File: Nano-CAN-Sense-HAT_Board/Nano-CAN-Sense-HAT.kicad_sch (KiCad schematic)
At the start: 44 parts, among them J1 Analog, J2 Digital, J3 Conn_02x04_Counter_Clockwise, J4 Conn_02x04_Counter_Clockwise, J5 Conn_01x05, J6 Conn_01x03, SW1 SW_Push, SW2 SW_Push, U1 LMC6484, U2 MCP2518FD-xQBB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

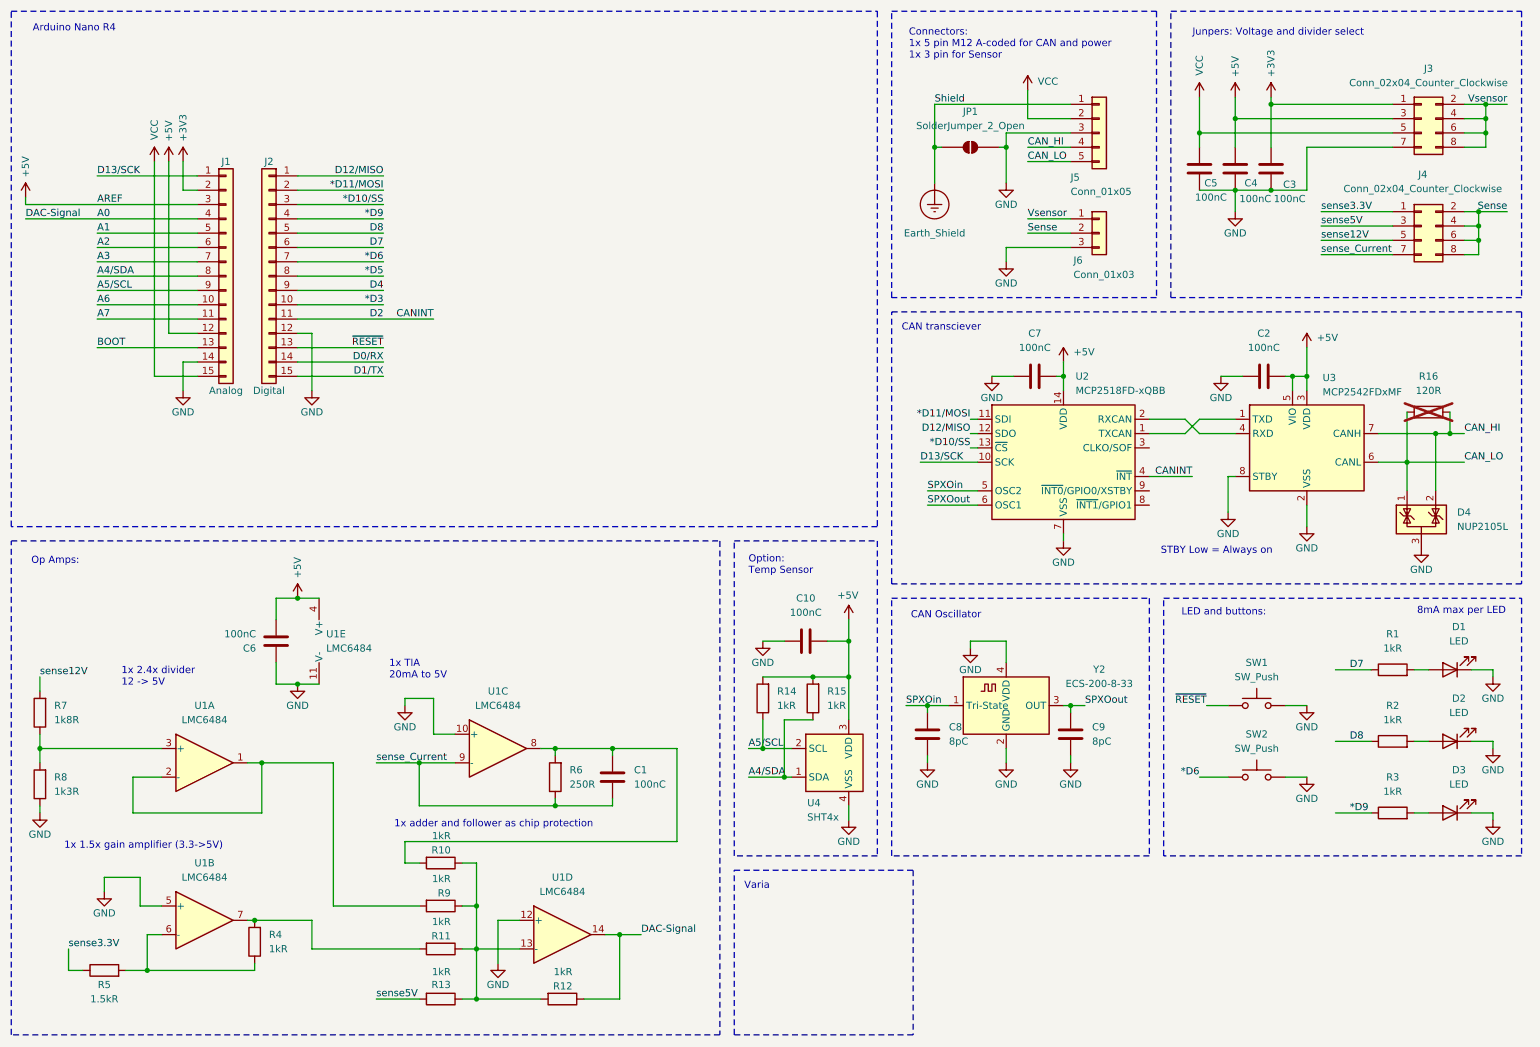
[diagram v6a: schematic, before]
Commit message: Changed OpAmp, improved lables
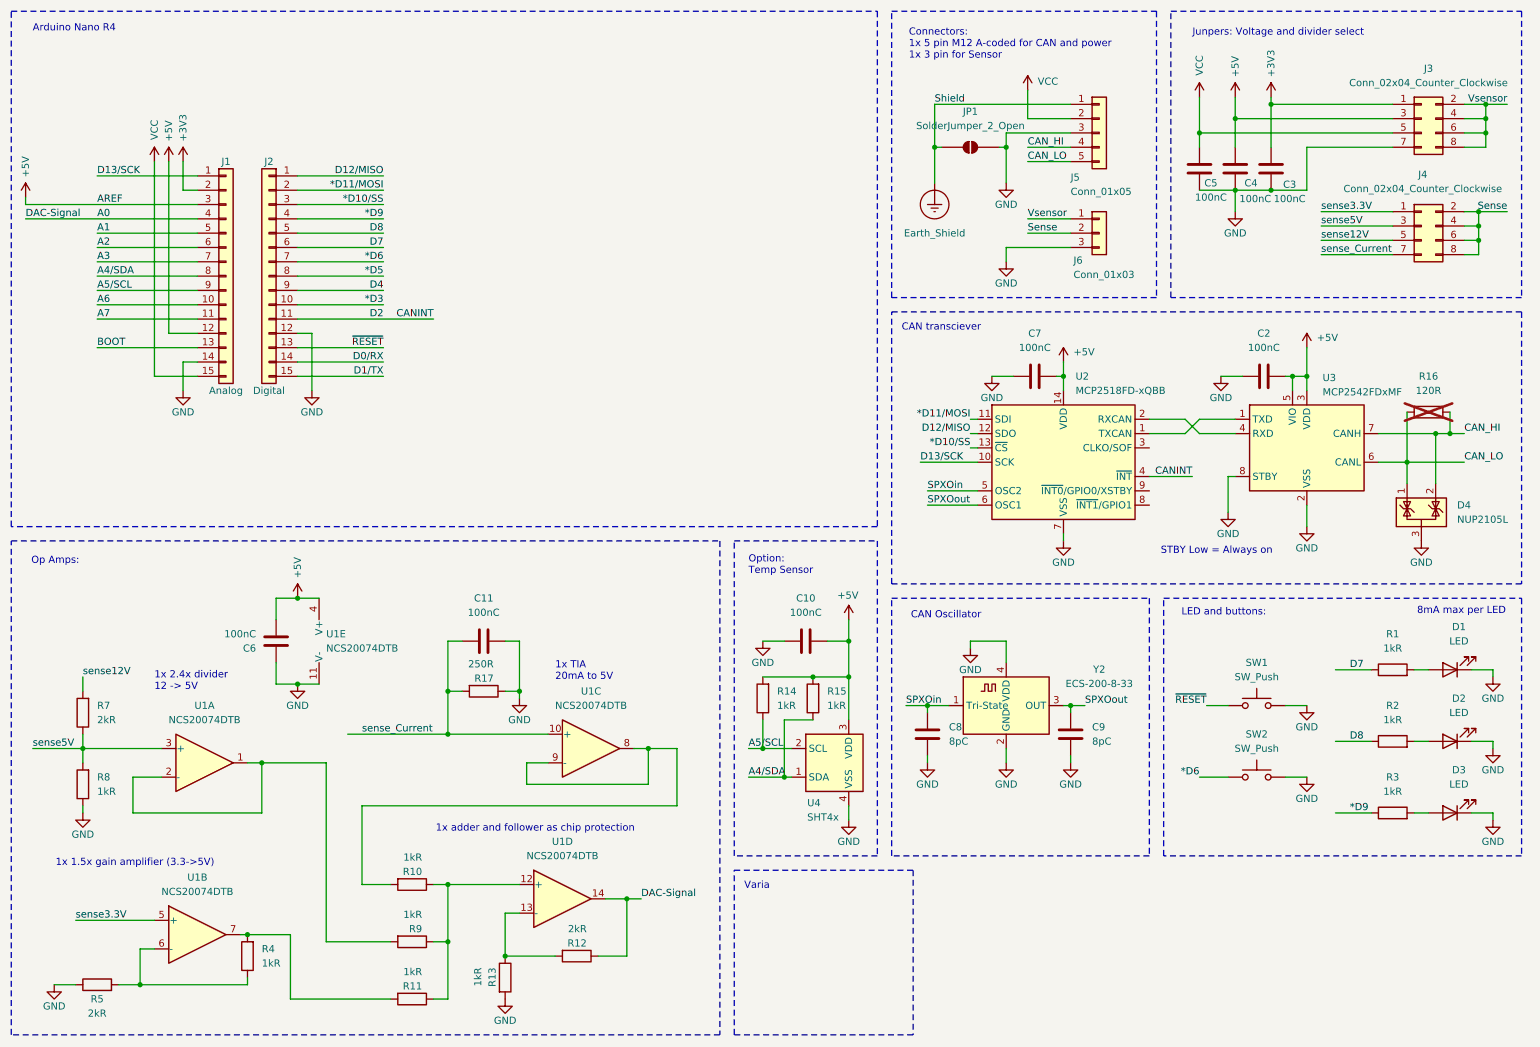
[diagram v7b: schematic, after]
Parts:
- removed C1: 100nC, Capacitor_SMD:C_0603_1608Metric, symbol Device:C
- removed R6: 250R, Resistor_SMD:R_0603_1608Metric, symbol Device:R
- added C11: 100nC, Capacitor_SMD:C_0603_1608Metric, symbol Device:C
- added R17: 250R, Resistor_SMD:R_0603_1608Metric, symbol Device:R
- R12: value 1kR -> 2kR
- R5: value 1.5kR -> 2kR
- R7: value 1k8R -> 2kR
- R8: value 1k3R -> 1kR
- U1: value LMC6484 -> NCS20074DTB; symbol Amplifier_Operational:LMC6484 -> Amplifier_Operational:NCS20074DTB
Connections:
- net GND: now also R13.2, R5.1, C11.2, R17.1; no longer U1.10 (+), U1.12 (+), U1.5 (+)
- net sense3.3V: now also U1.5 (+); no longer R5.1
- net sense5V: now also R7.1, R8.2, U1.3 (+); no longer R13.2
- net sense_Current: now also U1.10 (+), C11.1, R17.2; no longer U1.9 (-)
- net at R10.1, R11.1, R9.1: now also U1.12 (+); no longer R12.2, R13.1, U1.13 (-)
- net at R10.2, U1.8: now also U1.9 (-)
- new net: R12.2, R13.1, U1.13 (-)
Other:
- moved on the sheet: D4, R10, R11, R12, R4, R5, R7, R8, R9, U1B, U1C, U1D

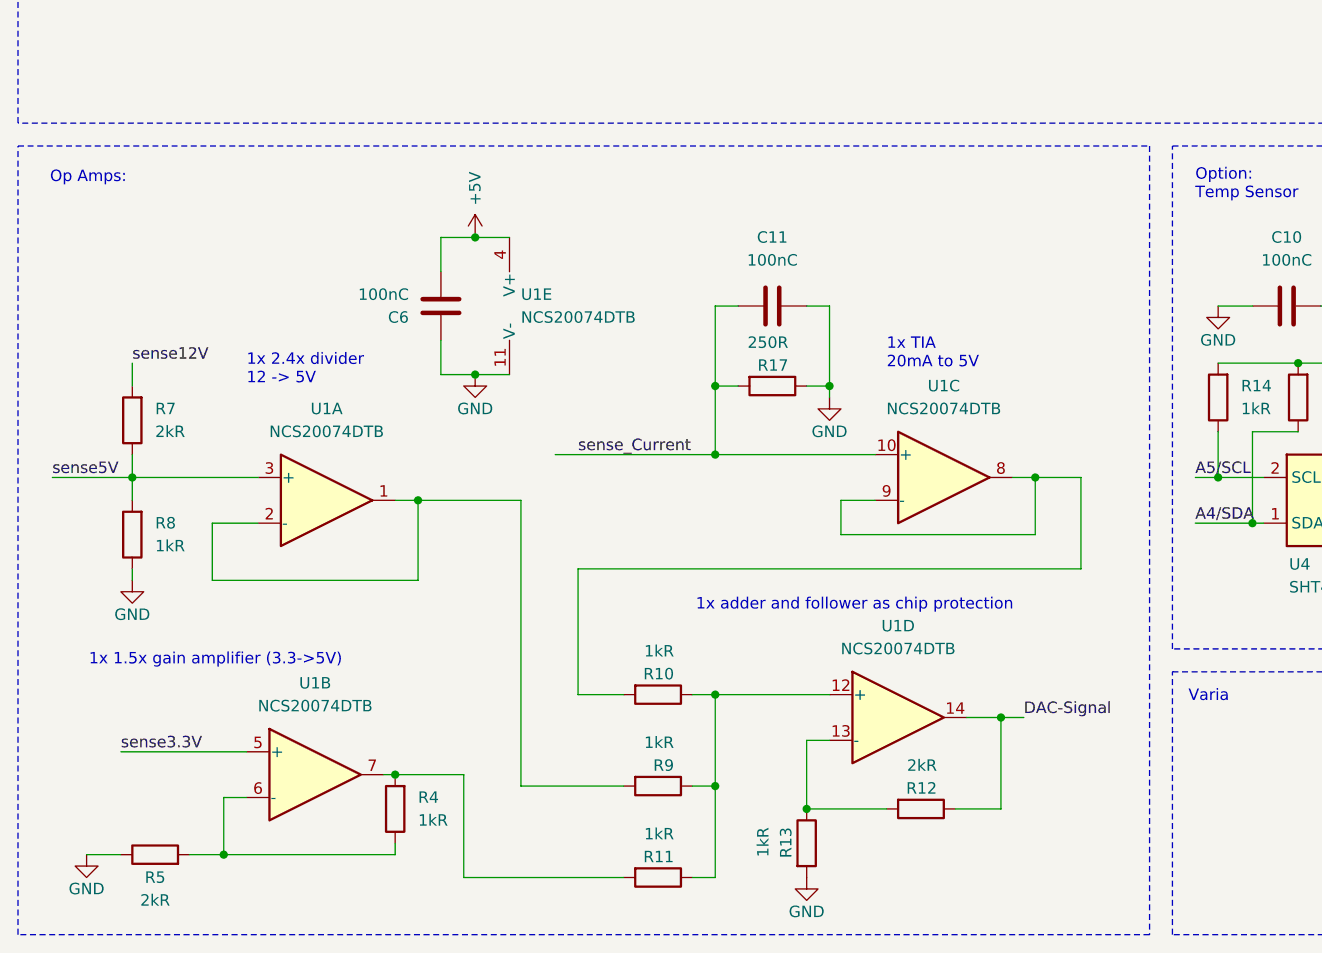
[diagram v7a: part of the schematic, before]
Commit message: Opamp supply 12V, Added Zener for protection
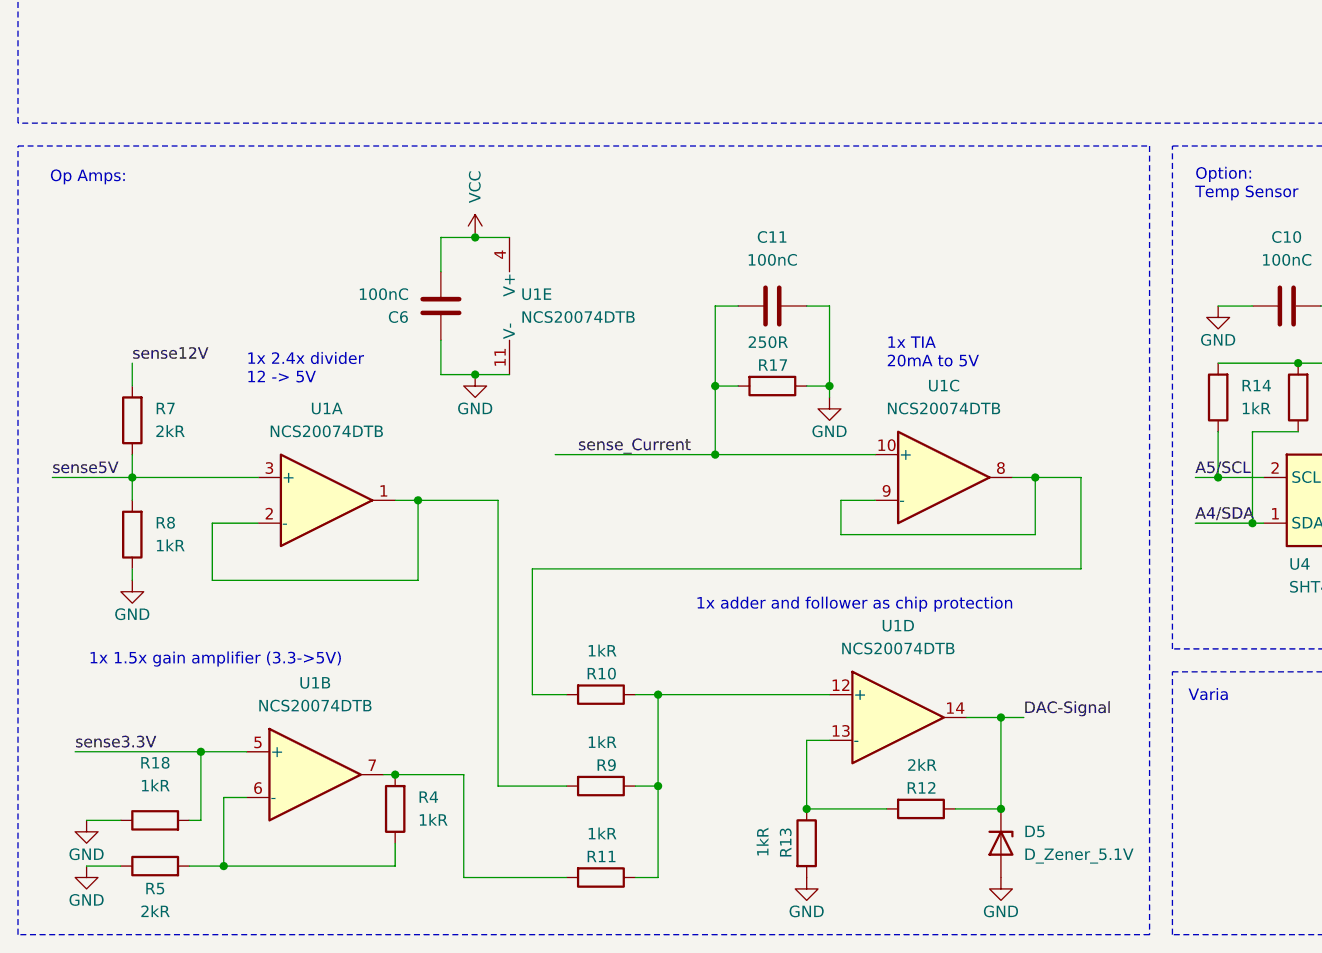
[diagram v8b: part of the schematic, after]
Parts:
- added D5: D_Zener_5.1V, Diode_SMD:D_SOD-323, symbol Device:D_Zener
- added R18: 1kR, Resistor_SMD:R_0603_1608Metric, symbol Device:R
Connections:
- net +5V: no longer C6.1, U1.4 (V+)
- net A0: now also D5.1 (K)
- net GND: now also D5.2 (A), R18.1
- net VCC: now also C6.1, U1.4 (V+)
- net sense3.3V: now also R18.2
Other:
- moved on the sheet: R10, R11, R5, R9
